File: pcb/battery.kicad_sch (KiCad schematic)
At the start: 25 parts, among them Q1 AO3400A, Q2 AO3401A, Q4 AO3401A, Q5 AO3400A, Q6 AO3401A, SW1 Power, U3 TP4056

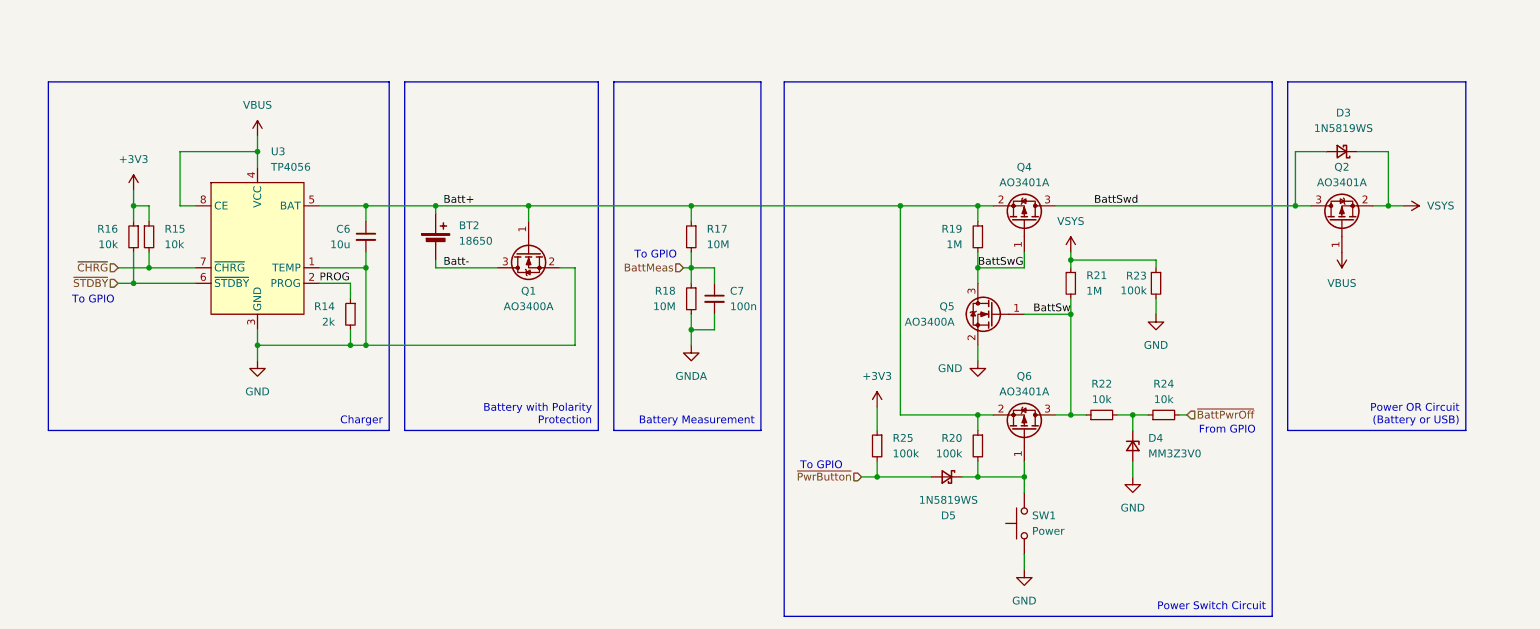
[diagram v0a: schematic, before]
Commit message: fix: replace buzzer footprint
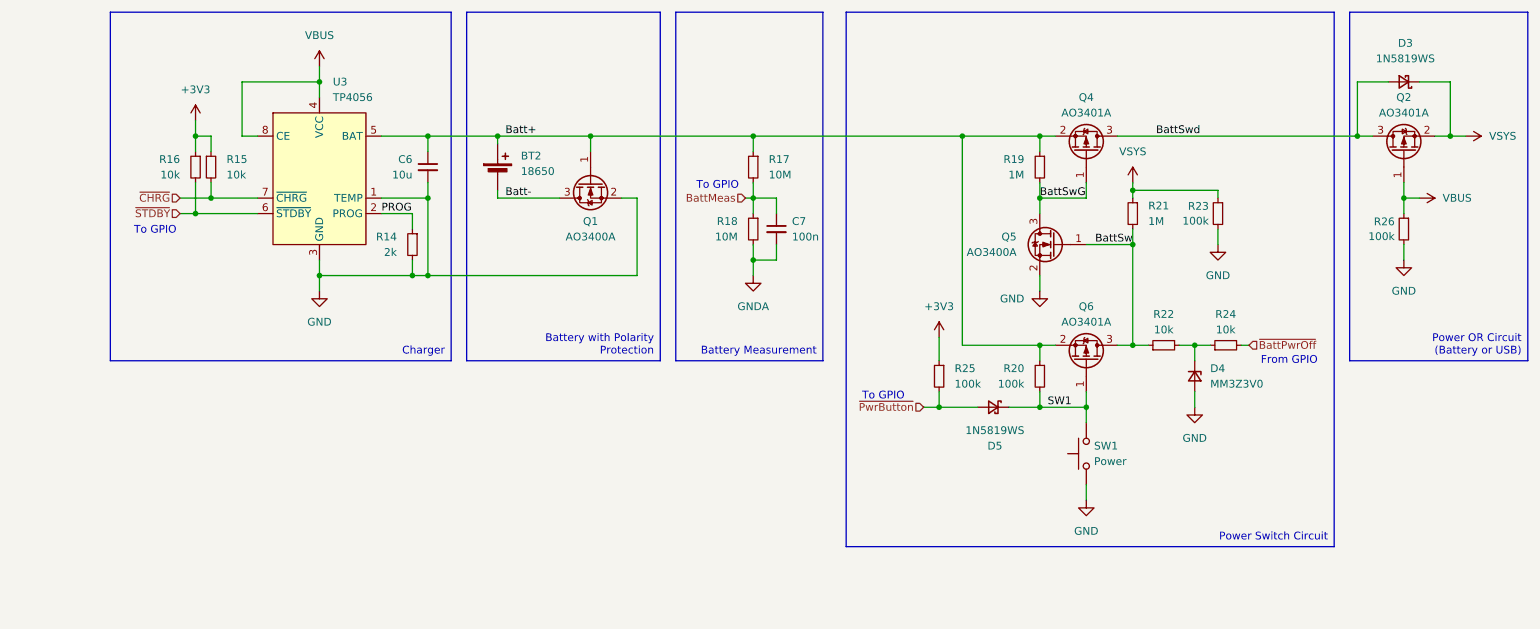
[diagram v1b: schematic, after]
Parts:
- added R26: 100k, Resistor_SMD:R_0402_1005Metric, symbol Device:R_Small
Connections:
- net GND: now also R26.2
- net VBUS: now also R26.1
- net SW1: now reaches D5.1 (K), Q6.1 (G), R20.2, SW1.2
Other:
- moved on the sheet: BT2, C6, C7, D3, D4, D5, Q1, Q2, Q4, Q5, Q6, R14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

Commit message: feat: place power button on the board
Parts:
- SW1: footprint Connector_JST:JST_PH_B2B-PH-K_1x02_P2.00mm_Vertical -> Button_Switch_THT:SW_Tactile_SPST_Angled_PTS645Vx58-2LFS
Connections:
- net GND: now also SW1.2; no longer SW1.1
- net SW1: now also SW1.1; no longer SW1.2
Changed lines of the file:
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@@
 		(lib_id "Switch:SW_Push")
 		(at 191.77 105.41 90)
+		(mirror x)
 		(unit 1)
 		(exclude_from_sim no)
@@
 			)
 		)
-		(property "Footprint" "Connector_JST:JST_PH_B2B-PH-K_1x02_P2.00mm_Vertical"
+		(property "Footprint" "Button_Switch_THT:SW_Tactile_SPST_Angled_PTS645Vx58-2LFS"
 			(at 186.69 105.41 0)
 			(effects

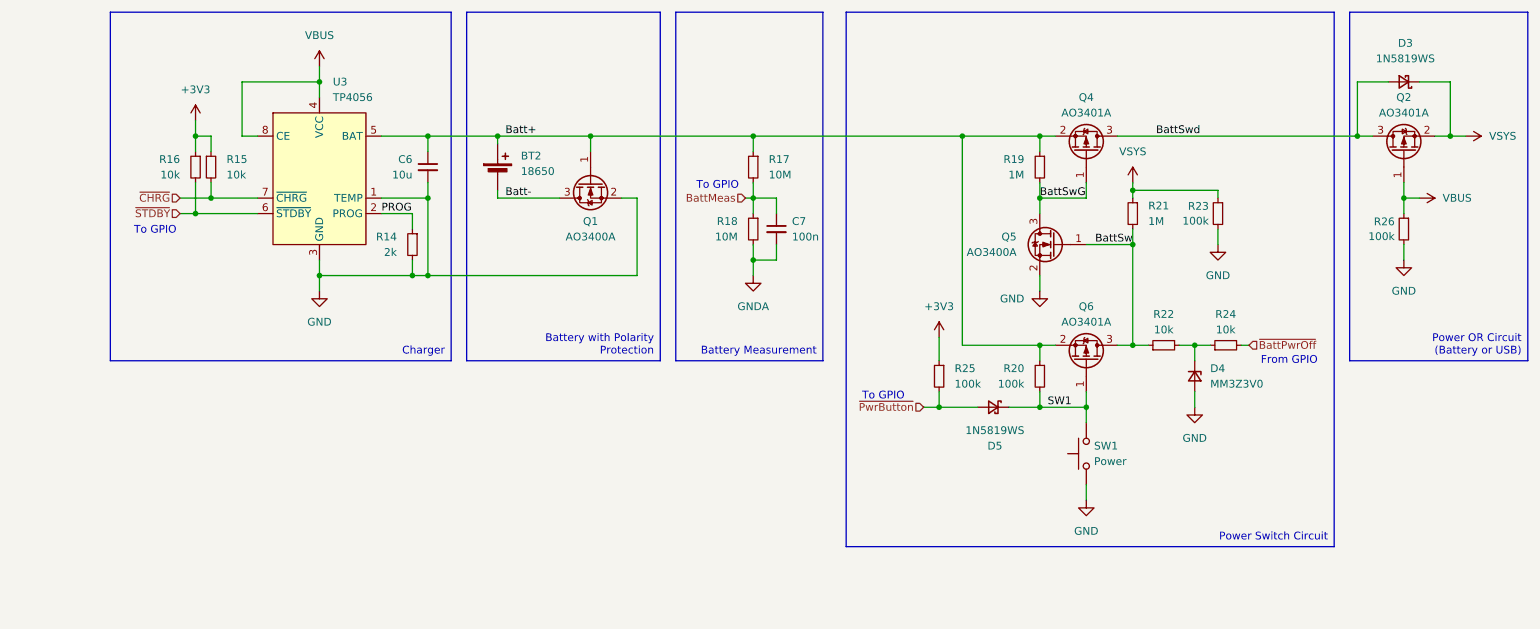
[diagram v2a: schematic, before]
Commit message: fix: add FET to measurement circuit
Disable the battery measurement circuit when the device is switched off to save energy
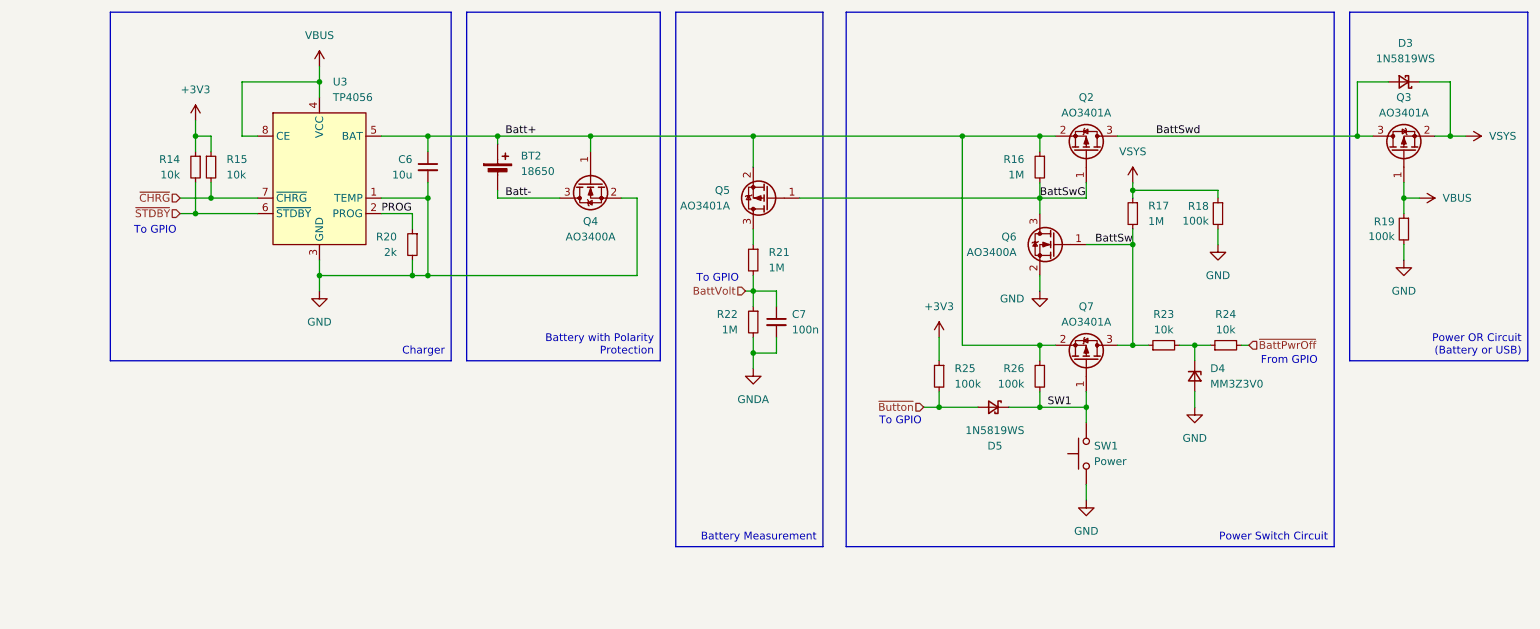
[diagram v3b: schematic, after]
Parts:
- added Q5: AO3401A, Package_TO_SOT_SMD:SOT-23, symbol Transistor_FET:AO3401A
- R21: renamed from R17; value 10M -> 1M; LCSC C26082 -> C26083
- R22: renamed from R18; value 10M -> 1M; LCSC C26082 -> C26083
- renumbered Q4 to Q2, Q2 to Q3, Q1 to Q4, Q5 to Q6, Q6 to Q7, R16 to R14, R19 to R16, R21 to R17, R23 to R18, R26 to R19, R14 to R20, R22 to R23, R20 to R26
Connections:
- net Batt+: now also Q5.2 (S); no longer R21.1
- net BattSwG: now also Q5.1 (G)
- net BattMeas renamed BattVolt
- net ~{PwrButton} renamed ~{Button}
- new net: Q5.3 (D), R21.1
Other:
- moved on the sheet: C7, R21, R22

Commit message: fix: power switch circuit capacitance
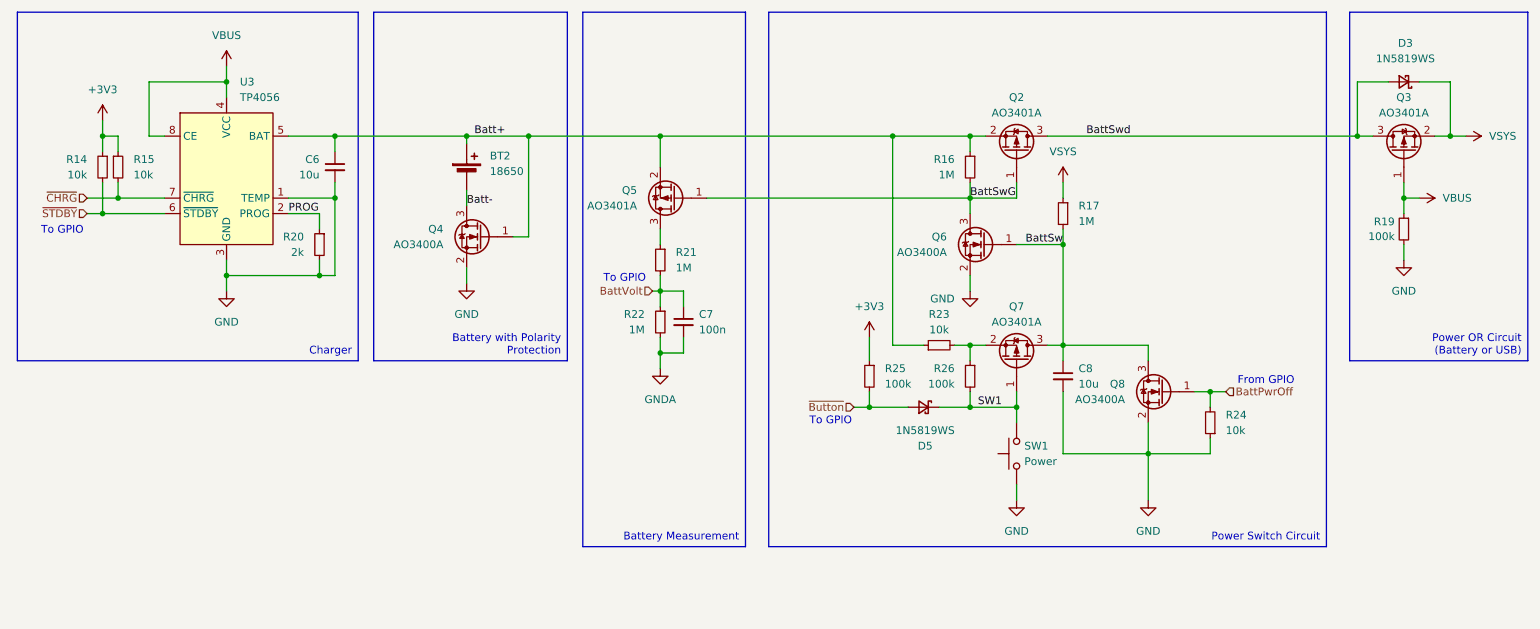
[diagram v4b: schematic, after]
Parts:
- removed D4: MM3Z3V0, Diode_SMD:D_SOD-323, symbol Device:D_Zener_Small
- removed R18: 100k, Resistor_SMD:R_0402_1005Metric, symbol Device:R_Small
- added C8: 10u, Capacitor_SMD:C_0402_1005Metric, symbol Device:C_Small
- added Q8: AO3400A, Package_TO_SOT_SMD:SOT-23, symbol Transistor_FET:AO3400A
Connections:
- net Batt+: now also R23.1; no longer Q7.2 (S), R26.1
- net BattSw: now also C8.1, Q8.3 (D); no longer R23.1
- net GND: now also R24.1, C8.2, Q8.2 (S)
- net at R23.2: now also Q7.2 (S), R26.1; no longer R24.1
- net ~{BattPwrOff} renamed BattPwrOff
- net BattPwrOff: now also Q8.1 (G)
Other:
- moved on the sheet: BT2, C6, C7, D5, Q2, Q4, Q5, Q6, Q7, R14, R15, R16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

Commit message: style: add some netclasses for schematic clarity
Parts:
- R22: renamed from R23; value 10k -> 1k; LCSC C25744 -> C11702
- renumbered D5 to D4, Q5 to Q4, Q4 to Q5, R19 to R18, R20 to R19, R21 to R20, R22 to R21, R25 to R23, R26 to R24, R24 to R25
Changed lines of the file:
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@@
 		(on_board yes)
 		(dnp no)
-		(property "Reference" "R19"
+		(property "Reference" "R18"
 			(at 242.3414 67.3679 0)
 			(effects
@@
 			(project "Badge-Scanner"
 				(path "/e99cd76d-c117-4654-ad48-596a9e3de149/0a7a7e59-ee25-477c-a5be-167264b2ebb9"
-					(reference "R19")
+					(reference "R18")
 					(unit 1)
 				)
@@
 		(dnp no)
 		(fields_autoplaced yes)
-		(property "Reference" "R25"
+		(property "Reference" "R23"
 			(at 158.75 91.4399 0)
 			(effects
@@
 			(project "Badge-Scanner"
 				(path "/e99cd76d-c117-4654-ad48-596a9e3de149/0a7a7e59-ee25-477c-a5be-167264b2ebb9"
-					(reference "R25")
+					(reference "R23")
 					(unit 1)
 				)
@@
 		(dnp no)
 		(fields_autoplaced yes)
-		(property "Reference" "#PWR051"
+		(property "Reference" "#PWR043"
 			(at 90.17 83.82 0)
 			(effects
@@
 			(project "Badge-Scanner"
 				(path "/e99cd76d-c117-4654-ad48-596a9e3de149/0a7a7e59-ee25-477c-a5be-167264b2ebb9"
-					(reference "#PWR051")
+					(reference "#PWR043")
 					(unit 1)
 				)
@@
 		(on_board yes)
 		(dnp no)
-		(property "Reference" "R26"
+		(property "Reference" "R24"
 			(at 170.18 91.4399 0)
 			(effects
@@
 			(project "Badge-Scanner"
 				(path "/e99cd76d-c117-4654-ad48-596a9e3de149/0a7a7e59-ee25-477c-a5be-167264b2ebb9"
-					(reference "R26")
+					(reference "R24")
 					(unit 1)
 				)
@@
 		(dnp no)
 		(fields_autoplaced yes)
-		(property "Reference" "#PWR048"
+		(property "Reference" "#PWR049"
 			(at 201.93 119.38 0)
 			(effects
@@
 			(project "Badge-Scanner"
 				(path "/e99cd76d-c117-4654-ad48-596a9e3de149/0a7a7e59-ee25-477c-a5be-167264b2ebb9"
-					(reference "#PWR048")
+					(reference "#PWR049")
 					(unit 1)
 				)
@@
 		(dnp no)
 		(fields_autoplaced yes)
-		(property "Reference" "R23"
+		(property "Reference" "R22"
 			(at 167.64 82.55 90)
 			(effects
@@
 			)
 		)
-		(property "Value" "10k"
+		(property "Value" "1k"
 			(at 167.64 85.09 90)
 			(effects
@@
 			)
 		)
-		(property "LCSC" "C25744"
+		(property "LCSC" "C11702"
 			(at 167.64 87.63 0)
 			(effects
@@
 			(project ""
 				(path "/e99cd76d-c117-4654-ad48-596a9e3de149/0a7a7e59-ee25-477c-a5be-167264b2ebb9"
-					(reference "R23")
+					(reference "R22")
 					(unit 1)
 				)
@@
 		(on_board yes)
 		(dnp no)
-		(property "Reference" "D5"
+		(property "Reference" "D4"
 			(at 165.354 104.14 0)
 			(effects
@@
 			(project "Badge-Scanner"
 				(path "/e99cd76d-c117-4654-ad48-596a9e3de149/0a7a7e59-ee25-477c-a5be-167264b2ebb9"
-					(reference "D5")
+					(reference "D4")
 					(unit 1)
 				)
@@
 		(on_board yes)
 		(dnp no)
-		(property "Reference" "R20"
+		(property "Reference" "R19"
 			(at 63.5 69.8499 0)
 			(effects
@@
 			(project ""
 				(path "/e99cd76d-c117-4654-ad48-596a9e3de149/0a7a7e59-ee25-477c-a5be-167264b2ebb9"
-					(reference "R20")
+					(reference "R19")
 					(unit 1)
 				)
@@
 		(dnp no)
 		(fields_autoplaced yes)
-		(property "Reference" "#PWR043"
+		(property "Reference" "#PWR042"
 			(at 243.84 80.01 0)
 			(effects
@@
 			(project "Badge-Scanner"
 				(path "/e99cd76d-c117-4654-ad48-596a9e3de149/0a7a7e59-ee25-477c-a5be-167264b2ebb9"
-					(reference "#PWR043")
+					(reference "#PWR042")
 					(unit 1)
 				)
@@
 		(dnp no)
 		(fields_autoplaced yes)
-		(property "Reference" "Q4"
+		(property "Reference" "Q5"
 			(at 86.36 68.5799 0)
 			(effects
@@
 			(project ""
 				(path "/e99cd76d-c117-4654-ad48-596a9e3de149/0a7a7e59-ee25-477c-a5be-167264b2ebb9"
-					(reference "Q4")
+					(reference "Q5")
 					(unit 1)
 				)
@@
 		(dnp no)
 		(fields_autoplaced yes)
-		(property "Reference" "#PWR049"
+		(property "Reference" "#PWR048"
 			(at 180.34 119.38 0)
 			(effects
@@
 			(project ""
 				(path "/e99cd76d-c117-4654-ad48-596a9e3de149/0a7a7e59-ee25-477c-a5be-167264b2ebb9"
-					(reference "#PWR049")
+					(reference "#PWR048")
 					(unit 1)
 				)
@@
 		(dnp no)
 		(fields_autoplaced yes)
-		(property "Reference" "R24"
+		(property "Reference" "R25"
 			(at 214.63 99.0599 0)
 			(effects
@@
 			(project "Badge-Scanner"
 				(path "/e99cd76d-c117-4654-ad48-596a9e3de149/0a7a7e59-ee25-477c-a5be-167264b2ebb9"
-					(reference "R24")
+					(reference "R25")
 					(unit 1)
 				)
@@
 		(dnp no)
 		(fields_autoplaced yes)
-		(property "Reference" "Q5"
+		(property "Reference" "Q4"
 			(at 118.11 62.2299 0)
 			(effects
@@
 			(project "Badge-Scanner"
 				(path "/e99cd76d-c117-4654-ad48-596a9e3de149/0a7a7e59-ee25-477c-a5be-167264b2ebb9"
-					(reference "Q5")
+					(reference "Q4")
 					(unit 1)
 				)
@@
 		(dnp no)
 		(fields_autoplaced yes)
-		(property "Reference" "R21"
+		(property "Reference" "R20"
 			(at 124.46 72.3899 0)
 			(effects
@@
 			(project ""
 				(path "/e99cd76d-c117-4654-ad48-596a9e3de149/0a7a7e59-ee25-477c-a5be-167264b2ebb9"
-					(reference "R21")
+					(reference "R20")
 					(unit 1)
 				)
@@
 		(on_board yes)
 		(dnp no)
-		(property "Reference" "R22"
+		(property "Reference" "R21"
 			(at 119.38 82.5499 0)
 			(effects
@@
 			(project "Badge-Scanner"
 				(path "/e99cd76d-c117-4654-ad48-596a9e3de149/0a7a7e59-ee25-477c-a5be-167264b2ebb9"
-					(reference "R22")
-					(unit 1)
-				)
+					(reference "R21")
+					(unit 1)
+				)

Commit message: fix: remove wrong order number from SW1
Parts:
- SW1: LCSC C2319 -> (none)
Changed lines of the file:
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@@
 			)
 		)
-		(property "LCSC" "C2319"
+		(property "LCSC" ""
 			(at 180.34 105.41 0)
 			(effects

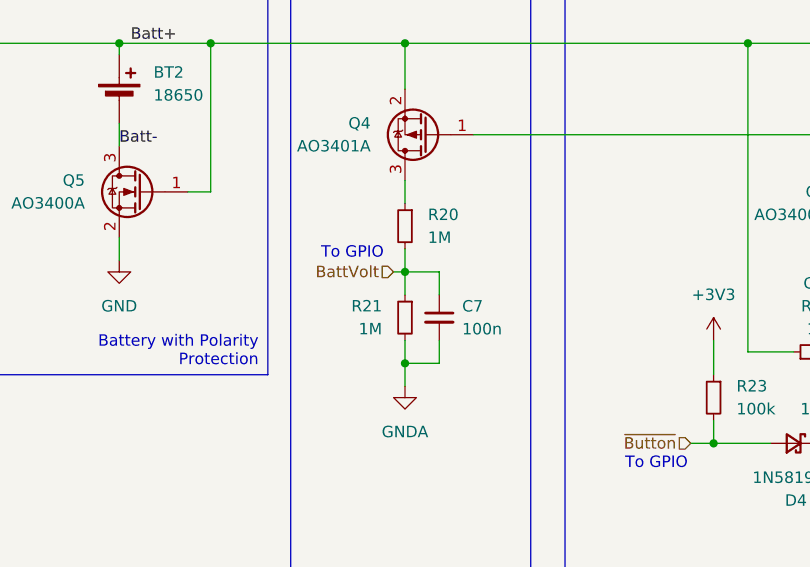
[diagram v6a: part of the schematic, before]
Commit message: fix: change resistor values for batt measurement
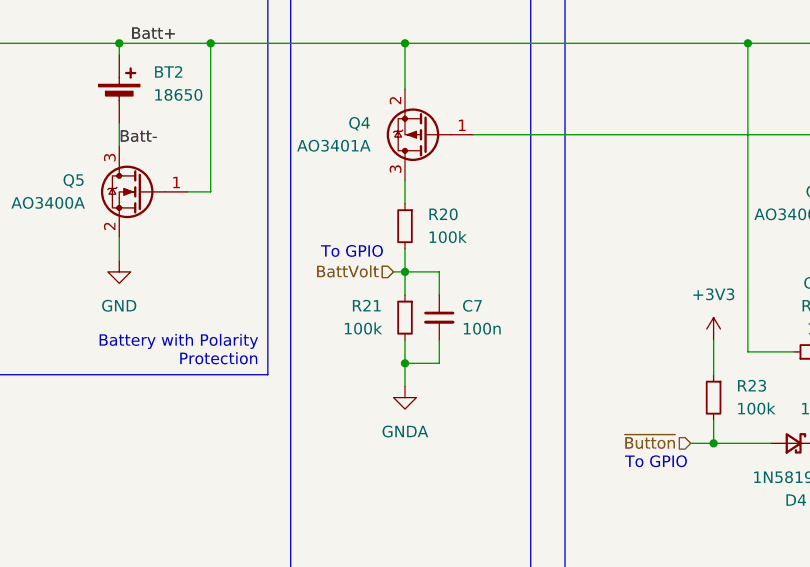
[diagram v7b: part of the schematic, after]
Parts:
- R20, R21: value 1M -> 100k; LCSC C26083 -> C25741
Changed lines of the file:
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@@
 			)
 		)
-		(property "Value" "1M"
+		(property "Value" "100k"
 			(at 124.46 74.9299 0)
 			(effects
@@
 			)
 		)
-		(property "LCSC" "C26083"
+		(property "LCSC" "C25741"
 			(at 121.92 73.66 0)
 			(effects
@@
 			)
 		)
-		(property "Value" "1M"
+		(property "Value" "100k"
 			(at 119.38 85.0899 0)
 			(effects
@@
 			)
 		)
-		(property "LCSC" "C26083"
+		(property "LCSC" "C25741"
 			(at 121.92 83.82 0)
 			(effects
